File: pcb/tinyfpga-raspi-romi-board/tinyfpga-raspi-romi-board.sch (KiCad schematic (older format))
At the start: 14 parts, among them J1 Conn_01x14_Female, J2 Conn_01x14_Female, J4 Conn_02x08_Odd_Even, J5 Conn_02x03_Odd_Even

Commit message: Added all headers connnecting the custom board to the romi pdb-mc board
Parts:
- added J? (x2): Conn_01x03_Female, symbol Connector:Conn_01x03_Female
- added J?: Conn_01x06_Female, symbol Connector:Conn_01x06_Female
- added J?: Conn_02x03_Odd_Even, symbol Connector_Generic:Conn_02x03_Odd_Even
- added J?: Conn_01x02_Female, Connector_PinHeader_1.27mm:PinHeader_1x02_P1.27mm_Vertical, symbol Connector:Conn_01x02_Female
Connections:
- net +5V: now also J?.2 (Pin_2)
- net GND: now also J?.14 (GND), J?.20 (GND), J?.25 (GND), J?.30 (GND), J?.34 (GND), J?.39 (GND), J?.6 (GND), J?.9 (GND), J?.2 (Pin_2), J?.3 (Pin_3), J?.3 (Pin_3), J?.4 (Pin_4), J?.6 (Pin_6)
- net at A?.2 (+VOUT), F?.2: now also J?.1 (Pin_1)
- new net ROMI_DIRL: J?.2 (Pin_2)
- new net ROMI_DIRR: J?.5 (Pin_5)
- new net ROMI_ENC_LA: J?.1 (Pin_1)
- new net ROMI_ENC_LB: J?.2 (Pin_2)
- new net ROMI_ENC_RA: J?.1 (Pin_1)
- new net ROMI_ENC_RB: J?.2 (Pin_2)
- new net ROMI_PWML: J?.3 (Pin_3)
- new net ROMI_PWMR: J?.6 (Pin_6)
- new net ROMI_VSW: J?.1 (Pin_1), J?.3 (Pin_3), J?.5 (Pin_5)
- new net ROMI_~SLPL: J?.1 (Pin_1)
- new net ROMI_~SLPR: J?.4 (Pin_4)
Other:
- note added: "Jump the fuse. You feelin' lucky, punk?"
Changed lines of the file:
@@
 	4600 4800 4600 4650
 Wire Wire Line
-	4600 4650 4850 4650
-Wire Wire Line
-	5150 4650 5350 4650
+	4600 4650 4800 4650
+Wire Wire Line
+	5150 4650 5200 4650
 $Comp
 L power:+BATT #PWR?
@@
 Wire Wire Line
 	4300 4750 4300 4600
+$Comp
+L Connector:Conn_01x03_Female J?
+U 1 1 5CDA7574
+P 1500 6850
+F 0 "J?" H 1600 6950 50  0000 C CNN
+F 1 "Conn_01x03_Female" H 1950 6850 50  0000 C CNN
+F 2 "" H 1500 6850 50  0001 C CNN
+F 3 "~" H 1500 6850 50  0001 C CNN
+	1    1500 6850
+	-1   0    0    -1
+$EndComp
+Text Label 2250 6750 2    50   ~ 0
+ROMI_ENC_LA
+Text Label 2250 7300 2    50   ~ 0
+ROMI_ENC_RA
+Text Label 2250 6850 2    50   ~ 0
+ROMI_ENC_LB
+Text Label 2250 7400 2    50   ~ 0
+ROMI_ENC_RB
+$Comp
+L Connector:Conn_01x03_Female J?
+U 1 1 5CDAB5A4
+P 1500 7400
+F 0 "J?" H 1550 7500 50  0000 L CNN
+F 1 "Conn_01x03_Female" H 1550 7400 50  0000 L CNN
+F 2 "" H 1500 7400 50  0001 C CNN
+F 3 "~" H 1500 7400 50  0001 C CNN
+	1    1500 7400
+	-1   0    0    -1
+$EndComp
+Wire Wire Line
+	1700 6750 2250 6750
+Wire Wire Line
+	2250 6850 1700 6850
+Wire Wire Line
+	2250 7300 1700 7300
+Wire Wire Line
+	2250 7400 1700 7400
+Wire Wire Line
+	1700 6950 1800 6950
+Wire Wire Line
+	1700 7500 1800 7500
+$Comp
+L power:GND #PWR?
+U 1 1 5CDB8BE2
+P 1800 6950
+F 0 "#PWR?" H 1800 6700 50  0001 C CNN
+F 1 "GND" H 1805 6777 50  0000 C CNN
+F 2 "" H 1800 6950 50  0001 C CNN
+F 3 "" H 1800 6950 50  0001 C CNN
+	1    1800 6950
+	-1   0    0    -1
+$EndComp
+$Comp
+L power:GND #PWR?
+U 1 1 5CDB91B9
+P 1800 7500
+F 0 "#PWR?" H 1800 7250 50  0001 C CNN
+F 1 "GND" H 1805 7327 50  0000 C CNN
+F 2 "" H 1800 7500 50  0001 C CNN
+F 3 "" H 1800 7500 50  0001 C CNN
+	1    1800 7500
+	1    0    0    -1
+$EndComp
+Wire Wire Line
+	2300 3650 2300 3750
+Wire Wire Line
+	2300 3750 2350 3750
+Wire Wire Line
+	3000 3750 3000 3650
+Wire Wire Line
+	2400 3650 2400 3750
+Connection ~ 2400 3750
+Wire Wire Line
+	2400 3750 2500 3750
+Connection ~ 2500 3750
+Wire Wire Line
+	2500 3750 2600 3750
+Wire Wire Line
+	2600 3750 2600 3650
+Connection ~ 2600 3750
+Wire Wire Line
+	2500 3650 2500 3750
+Wire Wire Line
+	2700 3650 2700 3750
+Wire Wire Line
+	2600 3750 2700 3750
+Connection ~ 2700 3750
+Wire Wire Line
+	2700 3750 2800 3750
+Wire Wire Line
+	2800 3650 2800 3750
+Connection ~ 2800 3750
+Wire Wire Line
+	2800 3750 2900 3750
+Wire Wire Line
+	2900 3650 2900 3750
+Connection ~ 2900 3750
+Wire Wire Line
+	2900 3750 3000 3750
+$Comp
+L power:GND #PWR?
+U 1 1 5CDD9BBB
+P 2350 3750
+F 0 "#PWR?" H 2350 3500 50  0001 C CNN
+F 1 "GND" H 2355 3577 50  0000 C CNN
+F 2 "" H 2350 3750 50  0001 C CNN
+F 3 "" H 2350 3750 50  0001 C CNN
+	1    2350 3750
+	-1   0    0    -1
+$EndComp
+Connection ~ 2350 3750
+Wire Wire Line
+	2350 3750 2400 3750
+$Comp
+L Connector:Conn_01x06_Female J?
+U 1 1 5CDDF928
+P 1500 6150
+F 0 "J?" H 1392 6535 50  0000 C CNN
+F 1 "Conn_01x06_Female" H 1900 6150 50  0000 C CNN
+F 2 "" H 1500 6150 50  0001 C CNN
+F 3 "~" H 1500 6150 50  0001 C CNN
+	1    1500 6150
+	-1   0    0    -1
+$EndComp
+$Comp
+L Connector_Generic:Conn_02x03_Odd_Even J?
+U 1 1 5CDE35EF
+P 1500 5100
+F 0 "J?" H 1550 5417 50  0000 C CNN
+F 1 "Conn_02x03_Odd_Even" H 1550 5326 50  0000 C CNN
+F 2 "" H 1500 5100 50  0001 C CNN
+F 3 "~" H 1500 5100 50  0001 C CNN
+	1    1500 5100
+	1    0    0    -1
+$EndComp
+Wire Wire Line
+	900  5000 1300 5000
+$Comp
+L power:GND #PWR?
+U 1 1 5CDEB28B
+P 1850 5250
+F 0 "#PWR?" H 1850 5000 50  0001 C CNN
+F 1 "GND" H 1855 5077 50  0000 C CNN
+F 2 "" H 1850 5250 50  0001 C CNN
+F 3 "" H 1850 5250 50  0001 C CNN
+	1    1850 5250
+	-1   0    0    -1
+$EndComp
+Wire Wire Line
+	1800 5000 1850 5000
+Wire Wire Line
+	1850 5000 1850 5100
+Wire Wire Line
+	1800 5200 1850 5200
+Connection ~ 1850 5200
+Wire Wire Line
+	1850 5200 1850 5250
+Wire Wire Line
+	1800 5100 1850 5100
+Connection ~ 1850 5100
+Wire Wire Line
+	1850 5100 1850 5200
+$Comp
+L Connector:Conn_01x02_Female J?
+U 1 1 5CDF3B4A
+P 4950 4200
+F 0 "J?" V 5100 4150 50  0000 L CNN
+F 1 "Conn_01x02_Female" V 5000 3850 50  0000 L CNN
+F 2 "Connector_PinHeader_1.27mm:PinHeader_1x02_P1.27mm_Vertical" H 4950 4200 50  0001 C CNN
+F 3 "~" H 4950 4200 50  0001 C CNN
+	1    4950 4200
+	0    -1   -1   0
+$EndComp
+Wire Wire Line
+	4950 4400 4800 4400
+Wire Wire Line
+	4800 4400 4800 4650
+Connection ~ 4800 4650
+Wire Wire Line
+	4800 4650 4850 4650
+Wire Wire Line
+	5050 4400 5200 4400
+Wire Wire Line
+	5200 4400 5200 4650
+Connection ~ 5200 4650
+Wire Wire Line
+	5200 4650 5350 4650
+Text Notes 4450 3950 0    50   ~ 0
+Jump the fuse. You feelin' lucky, punk?
+Text Label 2150 5950 2    50   ~ 0
+ROMI_~SLPL
+Text Label 2150 6250 2    50   ~ 0
+ROMI_~SLPR
+Text Label 2150 6050 2    50   ~ 0
+ROMI_DIRL
+Text Label 900  5000 0    50   ~ 0
+ROMI_VSW
+Text Label 900  5100 0    50   ~ 0
+ROMI_VSW
+Text Label 900  5200 0    50   ~ 0
+ROMI_VSW
+Wire Wire Line
+	900  5100 1300 5100
+Wire Wire Line
+	900  5200 1300 5200
+Text Label 2150 6150 2    50   ~ 0
+ROMI_PWML
+Text Label 2150 6450 2    50   ~ 0
+ROMI_PWMR
+Text Label 2150 6350 2    50   ~ 0
+ROMI_DIRR
+Wire Wire Line
+	1700 5950 2150 5950
+Wire Wire Line
+	2150 6050 1700 6050
+Wire Wire Line
+	1700 6150 2150 6150
+Wire Wire Line
+	2150 6250 1700 6250
+Wire Wire Line
+	1700 6350 2150 6350
+Wire Wire Line
+	2150 6450 1700 6450
 $EndSCHEMATC

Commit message: annotated the parts. woah. big change
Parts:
- gave numbers to parts that had none: 15
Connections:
- net ROMI_VSW is gone; now on net +BATT: J7.1 (Pin_1), J7.3 (Pin_3), J7.5 (Pin_5)
- net FPGA_3.3V: no longer J2.3 (Pin_3), J4.3 (Pin_3)
- net FPGA_5V: no longer J2.1 (Pin_1)
- net RPI_ID_SD: now reaches J3.27 (ID_SD/GPIO0)
- net RPI_ID_SD: now also R1.1, U1.5 (SDA)
- net RPI_ID_SC: now reaches J3.28 (ID_SC/GPIO1)
- net RPI_ID_SC: now also R2.1, U1.6 (SCL)
- new net FPGA_3.3V_OUT: J2.3 (Pin_3), J4.3 (Pin_3)
- new net FPGA_5V_IN: J2.1 (Pin_1)
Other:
- note added: "For doing device tree things.\nYou probably don't want to do device tree things."
- moved on the sheet: A1, D1, F1, J6, J8, R1, R2, R3, R4

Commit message: added sensor connectors. wired more or less everything together. broke out FPGA SPI flash pins
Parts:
- added C1: C_BULK, symbol Device:CP1
- added J12, J13, J14, J15: Conn_01x04_Female, symbol Connector:Conn_01x04_Female
- added R10, R9: 3.9k, Resistor_THT:R_Axial_DIN0204_L3.6mm_D1.6mm_P1.90mm_Vertical, symbol Device:R_US
- added R5, R6, R7, R8: 1k, Resistor_THT:R_Axial_DIN0204_L3.6mm_D1.6mm_P1.90mm_Vertical, symbol Device:R_US
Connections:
- net FPGA_5V_IN is gone; now on net +5V: J2.1 (Pin_1)
- net +3V3: now also J12.2 (Pin_2), J13.2 (Pin_2)
- net +5V: now also C1.1, J14.1 (Pin_1), J15.1 (Pin_1)
- net GND: now also J1.1 (Pin_1), C1.2, J12.3 (Pin_3), J13.3 (Pin_3), J14.4 (Pin_4), J15.4 (Pin_4), R10.1, R9.1; no longer J1.14 (Pin_14)
- net ROMI_DIRL: now also J2.6 (Pin_6)
- net ROMI_DIRR: now also J2.9 (Pin_9)
- net ROMI_ENC_LA: now also J2.11 (Pin_11)
- net ROMI_ENC_LB: now also J2.12 (Pin_12)
- net ROMI_ENC_RA: now also J2.13 (Pin_13)
- net ROMI_ENC_RB: now also J2.14 (Pin_14)
- net ROMI_PWML: now also J2.7 (Pin_7)
- net ROMI_PWMR: now also J2.10 (Pin_10)
- net ROMI_~SLPL: now also J2.5 (Pin_5)
- net ROMI_~SLPR: now also J2.8 (Pin_8)
- net RPI_RXD: now reaches J3.10 (GPIO15/RXD)
- net RPI_RXD: now also J1.6 (Pin_6)
- net FPGA_SDI: now reaches J3.19 (MOSI0/GPIO10)
- net FPGA_SDI: now also J4.12 (Pin_12)
- net FPGA_SDO: now reaches J3.21 (MISO0/GPIO9)
- net FPGA_SDO: now also J4.13 (Pin_13)
- net FPGA_SCK: now reaches J3.23 (SCLK0/GPIO11)
- net FPGA_SCK: now also J4.11 (Pin_11)
- net FPGA_SS: now reaches J3.24 (~CE0~/GPIO8)
- net FPGA_SS: now also J4.14 (Pin_14)
- net FPGA_~HOLD: now reaches J3.29 (GCLK1/GPIO5)
- net FPGA_~HOLD: now also J4.9 (Pin_9)
- net FPGA_~WP: now reaches J3.31 (GCLK2/GPIO6)
- net FPGA_~WP: now also J4.10 (Pin_10)
- net RPI_TXD: now reaches J3.8 (GPIO14/TXD)
- net RPI_TXD: now also J1.5 (Pin_5)
- net SONR_ECHO: now reaches J1.10 (Pin_10)
- net SONR_ECHO: now also J15.3 (Pin_3), R6.2
- net QTRR_CTRL: now reaches J1.11 (Pin_11)
- net QTRR_CTRL: now also J13.4 (Pin_4)
- net QTRR_OUT: now reaches J1.12 (Pin_12)
- net QTRR_OUT: now also J13.1 (Pin_1)
- net QTRL_CTRL: now reaches J1.13 (Pin_13)
- net QTRL_CTRL: now also J12.4 (Pin_4)
- net SONL_TRIG: now reaches J1.7 (Pin_7)
- net SONL_TRIG: now also J14.2 (Pin_2)
- net SONL_ECHO: now reaches J1.8 (Pin_8)
- net SONL_ECHO: now also J14.3 (Pin_3), R5.2
- net SONR_TRIG: now reaches J1.9 (Pin_9)
- net SONR_TRIG: now also J15.2 (Pin_2)
- new net: R5.1, R7.2
- new net: R6.1, R8.2
- new net QTRL_OUT: J1.14 (Pin_14), J12.1 (Pin_1)
- new net SONL_ECHO_DIV: R7.1, R9.2
- new net SONR_ECHO_DIV: R10.2, R8.1
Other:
- moved on the sheet: J4

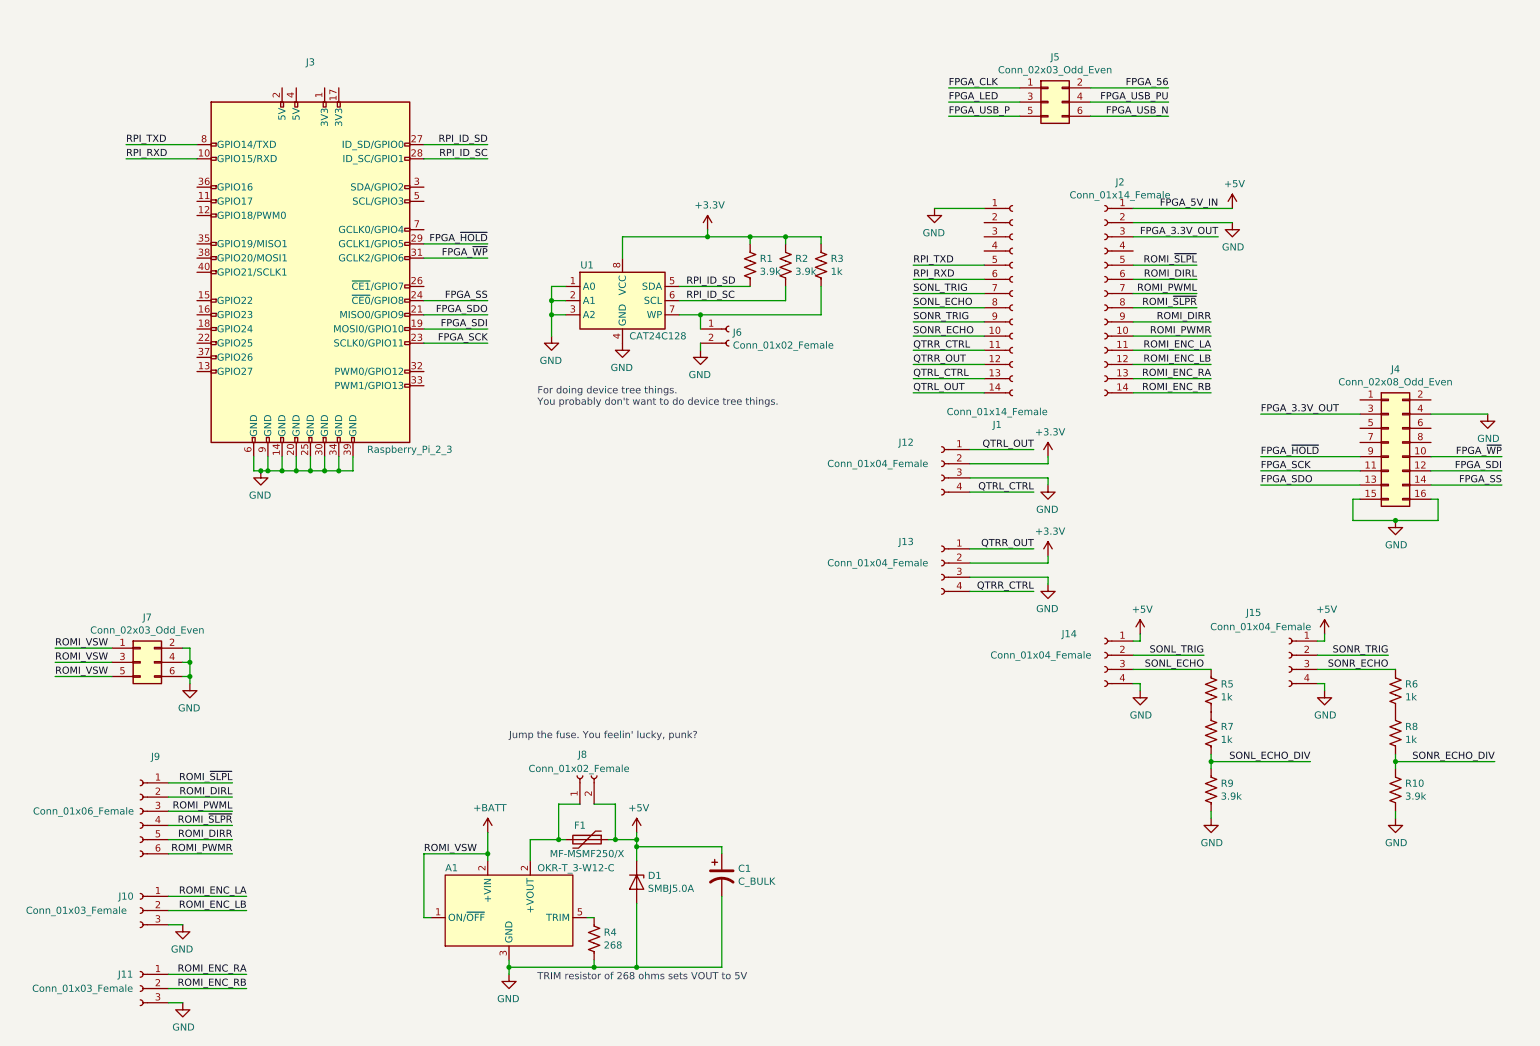
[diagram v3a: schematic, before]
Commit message: organization and labeling of hardware block
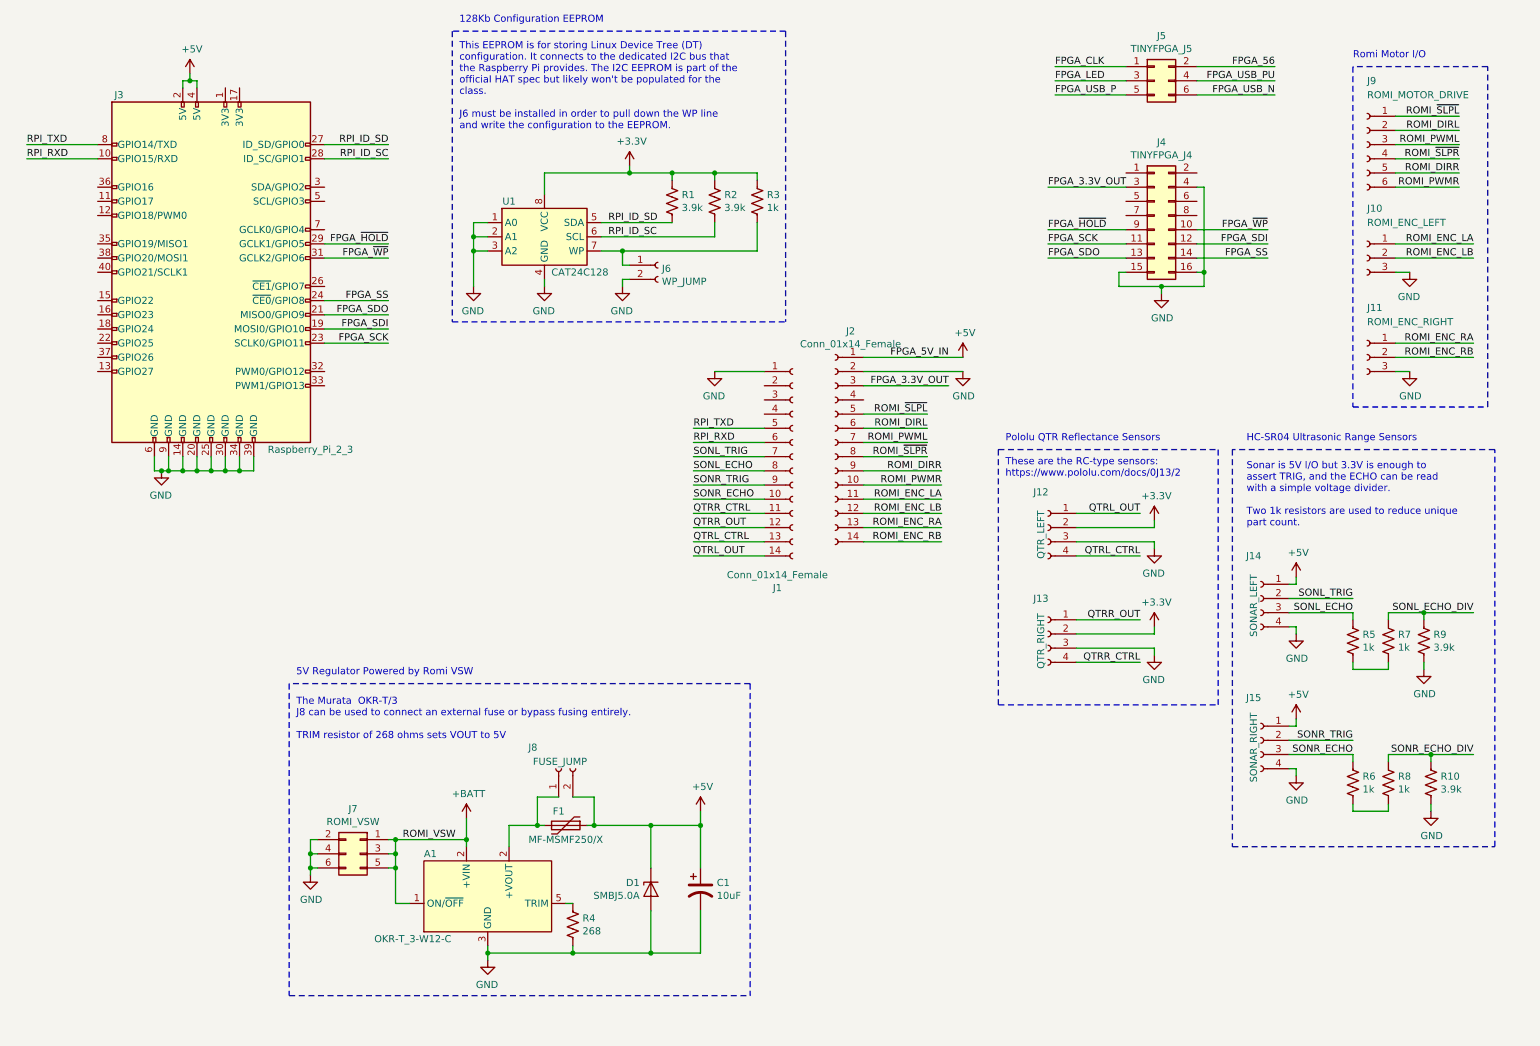
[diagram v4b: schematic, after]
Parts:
- C1: value C_BULK -> 10uF
- J10: value Conn_01x03_Female -> ROMI_ENC_LEFT
- J11: value Conn_01x03_Female -> ROMI_ENC_RIGHT
- J12: value Conn_01x04_Female -> QTR_LEFT
- J13: value Conn_01x04_Female -> QTR_RIGHT
- J14: value Conn_01x04_Female -> SONAR_LEFT
- J15: value Conn_01x04_Female -> SONAR_RIGHT
- J4: value Conn_02x08_Odd_Even -> TINYFPGA_J4
- J5: value Conn_02x03_Odd_Even -> TINYFPGA_J5
- J6: value Conn_01x02_Female -> WP_JUMP
- J7: value Conn_02x03_Odd_Even -> ROMI_VSW
- J8: value Conn_01x02_Female -> FUSE_JUMP
- J9: value Conn_01x06_Female -> ROMI_MOTOR_DRIVE
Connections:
- net +5V: now also J3.2 (5V), J3.4 (5V)
- net SONL_ECHO_DIV: now also R7.2; no longer R7.1
- net SONR_ECHO_DIV: now also R8.2; no longer R8.1
- net at R5.1: now also R7.1; no longer R7.2
- net at R6.1: now also R8.1; no longer R8.2
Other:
- note added: "128Kb Configuration EEPROM"
- note added: "5V Regulator Powered by Romi VSW"
- note added: "HC-SR04 Ultrasonic Range Sensors"
- note added: "Pololu QTR Reflectance Sensors"
- note added: "Romi Motor I/O"
- note added: "Sonar is 5V I/O but 3.3V is enough to\nassert TRIG, and the ECHO can be read\nwith a simple voltage divider.\n\nTwo 1k resistors are used to reduce unique\npart count."
- note added: "The Murata OKR-T/3 \nJ8 can be used to connect an external fuse or bypass fusing entirely.\n\nTRIM resistor of 268 ohms sets VOUT to 5V"
- note added: "These are the RC-type sensors:\nhttps://www.pololu.com/docs/0J13/2"
- note added: "This EEPROM is for storing Linux Device Tree (DT)\nconfiguration. It connects to the dedicated I2C bus that\nthe Raspberry Pi provides. The I2C EEPROM is part of the\nofficial HAT spec but likely won't be populated for the\nclass.\n\nJ6 must be installed in order to pull down the WP line\nand write the configuration to the EEPROM."
- note removed: "For doing device tree things.\nYou probably don't want to do device tree things."
- note removed: "Jump the fuse. You feelin' lucky, punk?"
- note removed: "TRIM resistor of 268 ohms sets VOUT to 5V"
- moved on the sheet: A1, C1, D1, F1, J1, J10, J11, J12, J13, J14, J15, J2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

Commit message: added some formatting for pres
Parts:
- added J16: PWR_SEL1, symbol Connector:Conn_01x03_Male
- added J17: PWR_SEL0, symbol Connector:Conn_01x03_Male
- J1: value Conn_01x14_Female -> TINYFPGA_J1
- J2: value Conn_01x14_Female -> TINYFPGA_J2
- J6, J8: symbol Connector:Conn_01x02_Female -> Connector:Conn_01x02_Male
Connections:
- net SONL_ECHO_DIV is gone; now on net SONL_ECHO: R7.2, R9.2
- net SONR_ECHO_DIV is gone; now on net SONR_ECHO: R10.2, R8.2
- net +3V3: now also J17.2 (Pin_2)
- net +5V: now also J8.1 (Pin_1); no longer J8.2 (Pin_2)
- net FPGA_3.3V_OUT: now also J16.1 (Pin_1)
- net SONL_ECHO: no longer J14.3 (Pin_3), R5.2
- net SONR_ECHO: no longer J15.3 (Pin_3), R6.2
- net RPI_3.3V_OUT: now reaches J3.1 (3V3)
- net RPI_3.3V_OUT: now also J3.17 (3V3), J16.3 (Pin_3)
- net FPGA_221: now reaches J1.2 (Pin_2)
- net FPGA_224: now reaches J1.3 (Pin_3)
- net FPGA_3A: now reaches J1.4 (Pin_4)
- net FPGA_185: now reaches J2.4 (Pin_4)
- net FPGA_140: now reaches J4.1 (Pin_1)
- net FPGA_24B: now reaches J4.2 (Pin_2)
- net FPGA_110: now reaches J4.5 (Pin_5)
- net FPGA_57: now reaches J4.6 (Pin_6)
- net FPGA_112: now reaches J4.7 (Pin_7)
- net FPGA_70: now reaches J4.8 (Pin_8)
- net at R5.1: now also J14.3 (Pin_3); no longer R7.1
- new net: A1.2 (+VOUT), F1.2, J8.2 (Pin_2)
- new net: J15.3 (Pin_3), R6.2
- new net: R5.2, R7.1
- new net: J16.2 (Pin_2), J17.1 (Pin_1)
- new net ROMI_3V3: J17.3 (Pin_3)
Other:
- note added: "3.3V Power Select Jumper"
- moved on the sheet: A1, C1, D1, F1, J1, J10, J11, J12, J13, J14, J15, J2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
